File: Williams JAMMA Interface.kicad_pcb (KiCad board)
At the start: 2 copper layers, 112.2 x 74.8 mm, 39 parts, among them P1 10K, U1 LM386, U2 DIP-14_W7.62mm_Socket, U3 MC34063AP

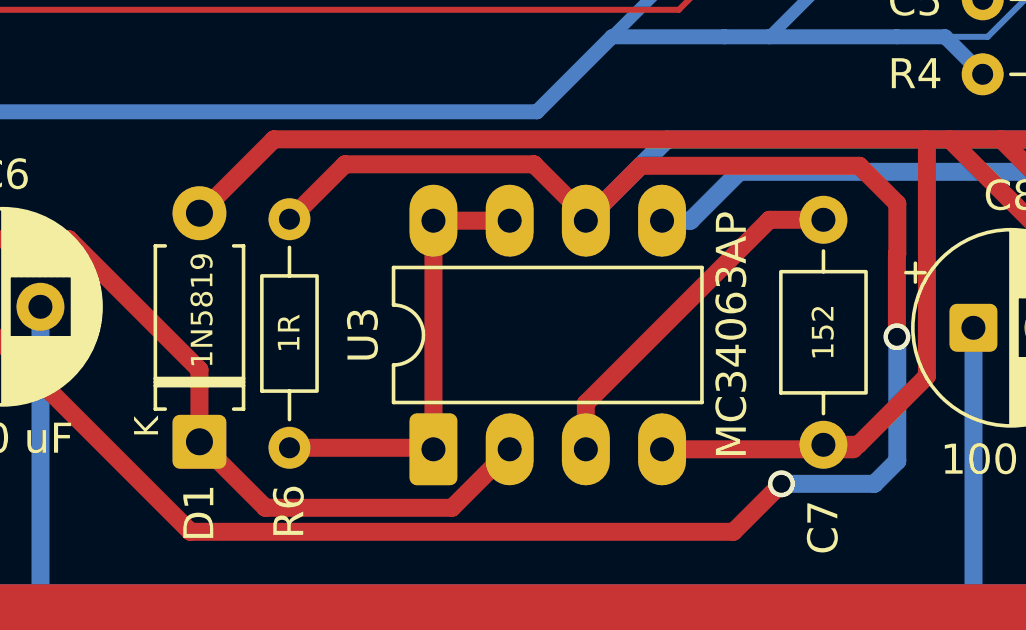
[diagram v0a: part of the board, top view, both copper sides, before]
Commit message: 152 becomes 2A152J (reduced noise)
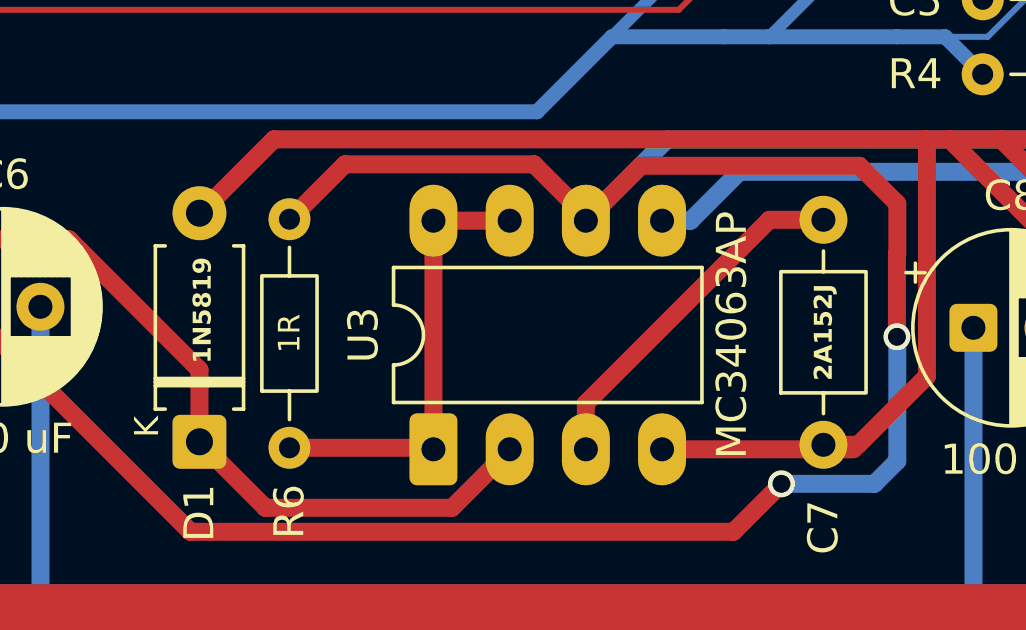
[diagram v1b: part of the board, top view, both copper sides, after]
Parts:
- C7: value 152 -> 2A152J
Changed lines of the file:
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@@
 			)
 		)
-		(property "Value" "152"
+		(property "Value" "2A152J"
 			(at 3.75 0 90)
 			(layer "F.SilkS")
 			(effects
 				(font
-					(size 0.72 0.72)
-					(thickness 0.108)
+					(size 0.6 0.6)
+					(thickness 0.1)
+					(bold yes)
 				)
 			)
@@
 			(effects
 				(font
-					(size 0.72 0.72)
-					(thickness 0.108)
+					(size 0.6 0.6)
+					(thickness 0.1)
+					(bold yes)
 				)
 			)

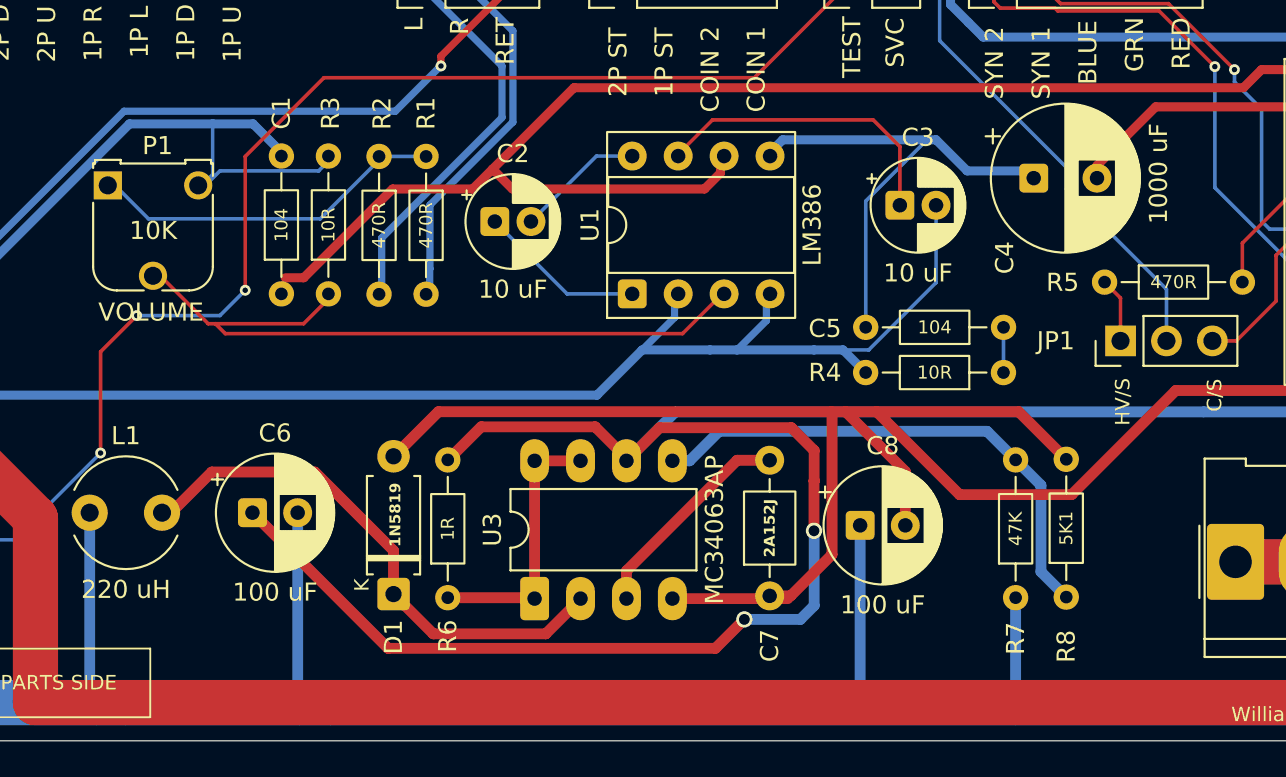
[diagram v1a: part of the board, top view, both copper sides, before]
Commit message: reduce form factor of C7, tweak layout and silkscreen
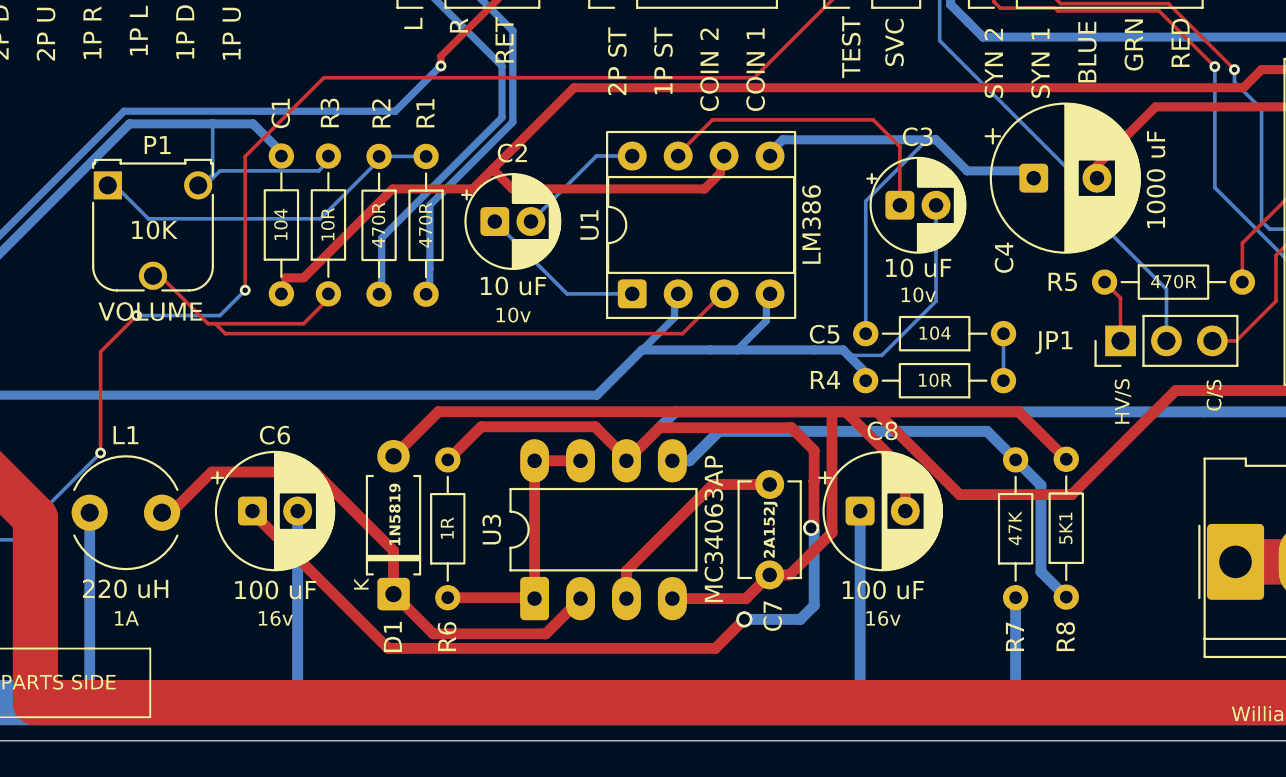
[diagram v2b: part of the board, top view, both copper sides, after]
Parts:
- C7: footprint Capacitor_THT:C_Axial_L3.8mm_D2.6mm_P7.50mm_Horizontal -> Capacitor_THT:C_Disc_D5.1mm_W3.2mm_P5.00mm
- moved C7 1.16 mm to (146.8, 128.9)
- moved C8 0.79 mm to (151.8, 125.4)
- moved R4 0.45 mm to (159.7, 118.2)
- moved C5 0.35 mm to (159.7, 115.6)
- moved C6 0.09 mm to (118.2, 125.4)
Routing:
- net -12V: track 142.1 -> 138.5 mm
- net U3_CAP: track 12.0 -> 11.4 mm
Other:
- board text added: "10v"
- board text added: "16v"
- board text added: "1A"
